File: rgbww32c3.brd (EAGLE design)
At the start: 36.8 x 20.3 mm, 21 parts, among them IC2 7805TV

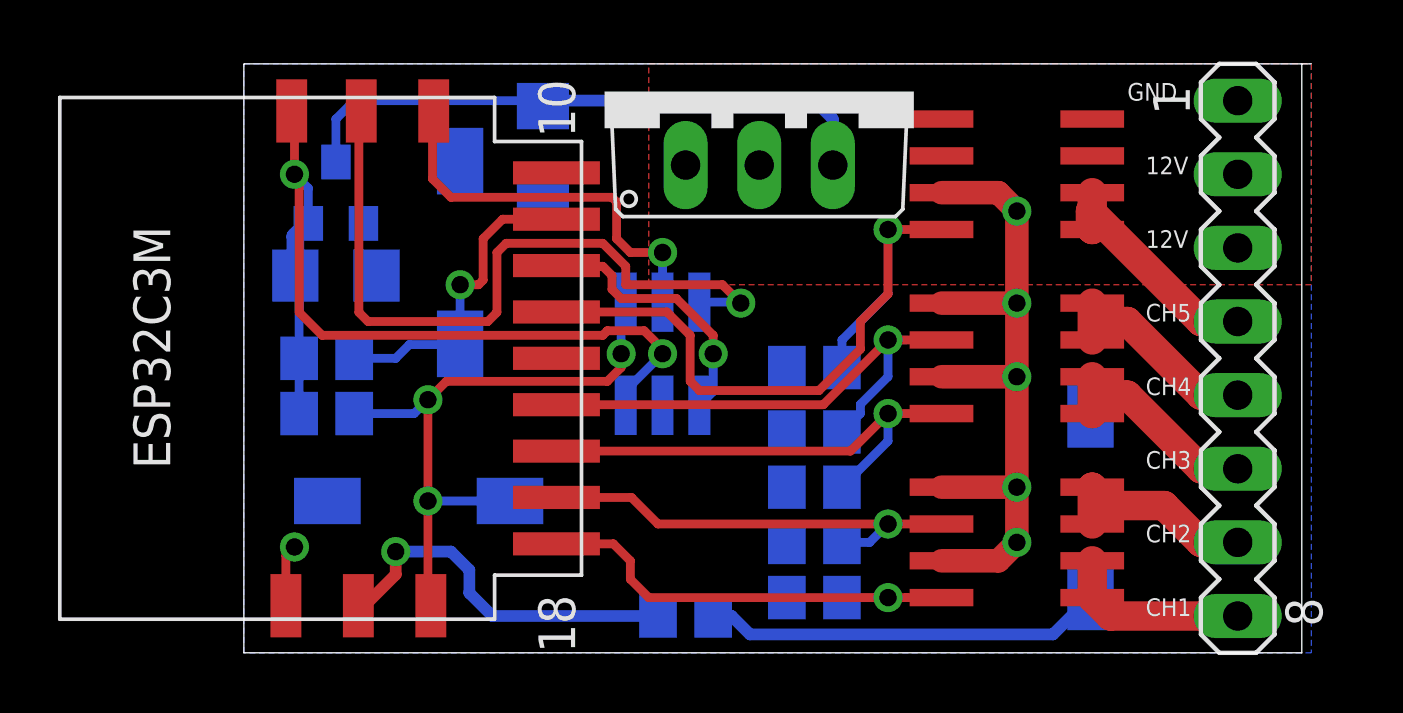
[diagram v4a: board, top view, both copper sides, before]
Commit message: few routing corrections to better avoid short circuits
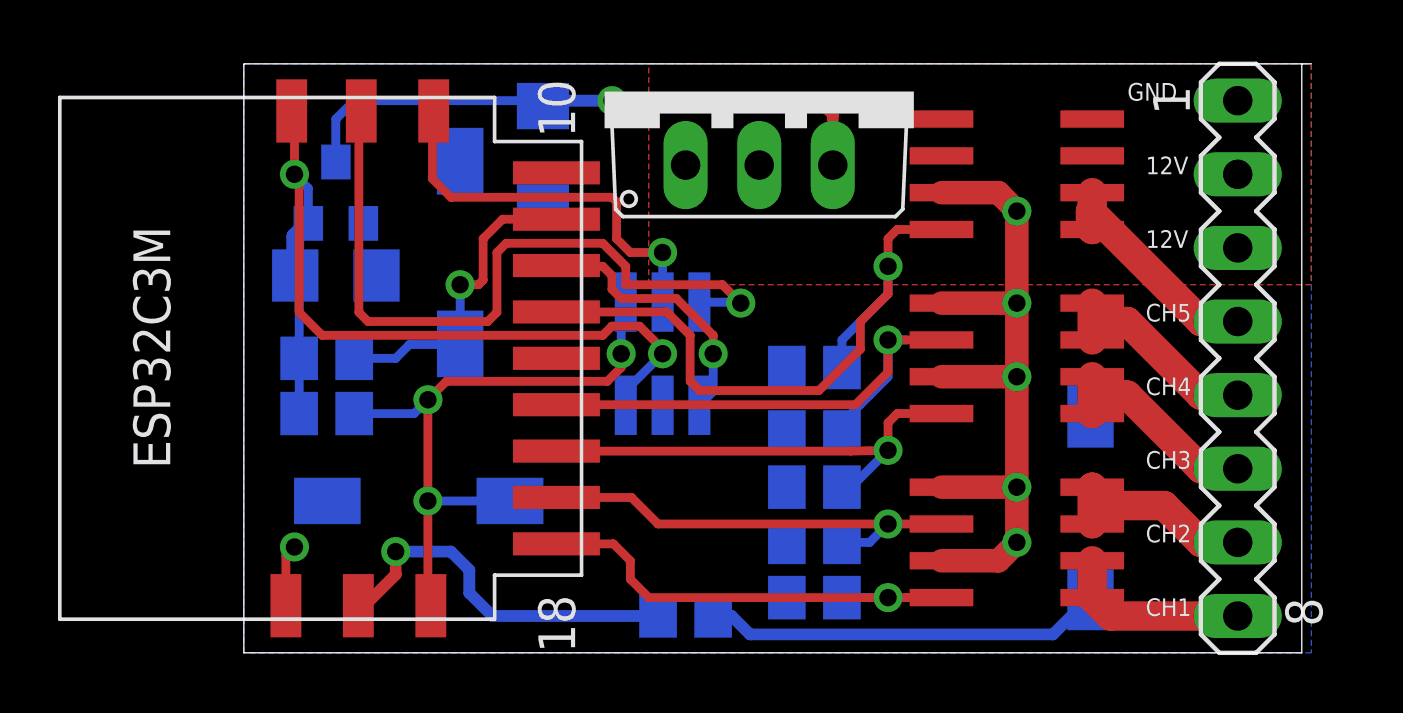
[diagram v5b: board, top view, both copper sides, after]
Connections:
- net CH1S: now also R4.1, U$1.4, U$5.GP10; no longer R3.1, U$1.2, U$5.GP7
- net CH2S: now also R3.1, U$1.2, U$5.GP7; no longer R4.1, U$1.4, U$5.GP10
- net CH3S: now also R2.1, U$2.4, U$5.GP6; no longer R5.1, U$2.2, U$5.GP5
- net CH4S: now also R5.1, U$2.2, U$5.GP5; no longer R2.1, U$2.4, U$5.GP6
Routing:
- net CH4S: track 17.0 -> 19.3 mm
- net CH3S: track 18.7 -> 16.5 mm
- net CH5S: track 24.9 -> 23.5 mm
- net 5V: track 21.0 -> 21.1 mm, vias 0 -> 1
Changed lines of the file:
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@@
 <contactref element="C2" pad="1"/>
 <wire x1="10.50625" y1="78.74" x2="10.31875" y2="78.5525" width="0.3048" layer="16"/>
-<wire x1="10.50625" y1="78.74" x2="19.685" y2="78.74" width="0.4064" layer="16"/>
-<wire x1="19.685" y1="78.74" x2="20.32" y2="78.105" width="0.4064" layer="16"/>
-<wire x1="20.32" y1="78.105" x2="20.32" y2="76.5175" width="0.4064" layer="16"/>
+<wire x1="10.50625" y1="78.74" x2="12.7" y2="78.74" width="0.4064" layer="16"/>
+<via x="12.7" y="78.74" extent="1-16" drill="0.6"/>
+<wire x1="12.7" y1="78.74" x2="19.84375" y2="78.74" width="0.4064" layer="1"/>
+<wire x1="19.84375" y1="78.74" x2="20.32" y2="78.26375" width="0.4064" layer="1"/>
+<wire x1="20.32" y1="78.26375" x2="20.32" y2="76.5175" width="0.4064" layer="1"/>
 </signal>
 <signal name="3V3">
@@
 <via x="14.44625" y="70.00875" extent="1-16" drill="0.6"/>
 <wire x1="14.44625" y1="70.00875" x2="14.44625" y2="70.1675" width="0.3048" layer="1"/>
-<wire x1="14.44625" y1="70.1675" x2="13.81125" y2="70.8025" width="0.3048" layer="1"/>
+<wire x1="14.44625" y1="70.1675" x2="13.6525" y2="70.96125" width="0.3048" layer="1"/>
 <wire x1="2.70125" y1="70.64375" x2="1.9075" y2="71.4375" width="0.3048" layer="1"/>
 <wire x1="1.9075" y1="71.4375" x2="1.9075" y2="76.03875" width="0.3048" layer="1"/>
 <wire x1="1.9075" y1="76.03875" x2="1.74625" y2="76.2" width="0.3048" layer="1"/>
-<wire x1="13.81125" y1="70.8025" x2="12.54125" y2="70.8025" width="0.3048" layer="1"/>
-<wire x1="12.54125" y1="70.8025" x2="12.3825" y2="70.64375" width="0.3048" layer="1"/>
+<wire x1="13.6525" y1="70.96125" x2="12.7" y2="70.96125" width="0.3048" layer="1"/>
+<wire x1="12.7" y1="70.96125" x2="12.3825" y2="70.64375" width="0.3048" layer="1"/>
 <wire x1="12.3825" y1="70.64375" x2="2.70125" y2="70.64375" width="0.3048" layer="1"/>
 <wire x1="1.775" y1="72.7075" x2="1.775" y2="74.055" width="0.6096" layer="16"/>
@@
 <via x="6.35" y="68.42125" extent="1-16" drill="0.6"/>
 </signal>
-<signal name="CH2S">
+<signal name="CH1S">
 <contactref element="R4" pad="1"/>
 <contactref element="U$1" pad="4"/>
@@
 <wire x1="22.225" y1="61.595" x2="20.635" y2="61.595" width="0.3048" layer="16"/>
 </signal>
-<signal name="CH1S">
+<signal name="CH2S">
 <contactref element="R3" pad="1"/>
 <contactref element="U$1" pad="2"/>
@@
 <wire x1="21.59" y1="63.5" x2="20.635" y2="63.5" width="0.3048" layer="16"/>
 </signal>
-<signal name="CH4S">
+<signal name="CH3S">
 <contactref element="R2" pad="1"/>
 <contactref element="U$2" pad="4"/>
 <contactref element="U$5" pad="GP6"/>
-<wire x1="24.07" y1="67.945" x2="22.225" y2="67.945" width="0.3048" layer="1"/>
-<via x="22.225" y="67.945" extent="1-16" drill="0.6"/>
+<via x="22.225" y="66.675" extent="1-16" drill="0.6"/>
 <wire x1="10.785" y1="66.65" x2="20.93" y2="66.65" width="0.3048" layer="1"/>
-<wire x1="20.93" y1="66.65" x2="22.225" y2="67.945" width="0.3048" layer="1"/>
-<wire x1="20.635" y1="65.405" x2="22.225" y2="66.995" width="0.3048" layer="16"/>
-<wire x1="22.225" y1="66.995" x2="22.225" y2="67.945" width="0.3048" layer="16"/>
+<wire x1="20.93" y1="66.65" x2="22.225" y2="66.675" width="0.3048" layer="1"/>
+<wire x1="24.07" y1="67.945" x2="22.5425" y2="67.945" width="0.3048" layer="1"/>
+<wire x1="22.5425" y1="67.945" x2="22.225" y2="67.6275" width="0.3048" layer="1"/>
+<wire x1="22.225" y1="67.6275" x2="22.225" y2="66.675" width="0.3048" layer="1"/>
+<wire x1="20.635" y1="65.405" x2="20.955" y2="65.405" width="0.3048" layer="16"/>
+<wire x1="20.955" y1="65.405" x2="22.225" y2="66.675" width="0.3048" layer="16"/>
 </signal>
-<signal name="CH3S">
+<signal name="CH4S">
 <contactref element="R5" pad="1"/>
 <contactref element="U$2" pad="2"/>
@@
 <wire x1="24.07" y1="70.485" x2="22.225" y2="70.485" width="0.3048" layer="1"/>
 <via x="22.225" y="70.485" extent="1-16" drill="0.6"/>
-<wire x1="10.785" y1="68.25" x2="19.99" y2="68.25" width="0.3048" layer="1"/>
-<wire x1="19.99" y1="68.25" x2="22.225" y2="70.485" width="0.3048" layer="1"/>
+<wire x1="10.785" y1="68.25" x2="21.10125" y2="68.25" width="0.3048" layer="1"/>
 <wire x1="22.225" y1="70.485" x2="22.86" y2="70.485" width="0.3048" layer="16"/>
-<wire x1="20.635" y1="67.31" x2="21.2725" y2="67.9475" width="0.3048" layer="16"/>
-<wire x1="21.2725" y1="67.9475" x2="21.2725" y2="68.2625" width="0.3048" layer="16"/>
-<wire x1="21.2725" y1="68.2625" x2="22.225" y2="69.215" width="0.3048" layer="16"/>
+<wire x1="21.2725" y1="68.2625" x2="21.59" y2="68.58" width="0.3048" layer="16"/>
+<wire x1="21.59" y1="68.58" x2="22.225" y2="69.215" width="0.3048" layer="16"/>
 <wire x1="22.225" y1="69.215" x2="22.225" y2="70.485" width="0.3048" layer="16"/>
+<wire x1="22.225" y1="70.485" x2="22.225" y2="69.37375" width="0.3048" layer="1"/>
+<wire x1="22.225" y1="69.37375" x2="21.10125" y2="68.25" width="0.3048" layer="1"/>
+<wire x1="20.635" y1="67.31" x2="20.635" y2="67.625" width="0.3048" layer="16"/>
+<wire x1="20.635" y1="67.625" x2="21.2725" y2="68.2625" width="0.3048" layer="16"/>
 </signal>
 <signal name="CH5S">
@@
 <contactref element="U$3" pad="4"/>
 <contactref element="U$5" pad="GP1"/>
-<wire x1="24.07" y1="74.295" x2="22.225" y2="74.295" width="0.3048" layer="1"/>
-<via x="22.225" y="74.295" extent="1-16" drill="0.6"/>
-<wire x1="22.225" y1="72.0725" x2="22.225" y2="74.295" width="0.3048" layer="16"/>
+<via x="22.225" y="73.025" extent="1-16" drill="0.6"/>
+<wire x1="22.225" y1="72.0725" x2="22.225" y2="73.025" width="0.3048" layer="16"/>
 <wire x1="20.635" y1="69.5325" x2="20.635" y2="70.4825" width="0.3048" layer="16"/>
 <wire x1="10.785" y1="71.45" x2="14.5925" y2="71.45" width="0.3048" layer="1"/>
@@
 <wire x1="21.2725" y1="70.1675" x2="21.2725" y2="71.12" width="0.3048" layer="1"/>
 <wire x1="21.2725" y1="71.12" x2="22.225" y2="72.0725" width="0.3048" layer="1"/>
-<wire x1="22.225" y1="72.0725" x2="22.225" y2="74.295" width="0.3048" layer="1"/>
+<wire x1="22.225" y1="72.0725" x2="22.225" y2="73.025" width="0.3048" layer="1"/>
+<wire x1="24.07" y1="74.295" x2="22.5425" y2="74.295" width="0.3048" layer="1"/>
+<wire x1="22.5425" y1="74.295" x2="22.225" y2="73.9775" width="0.3048" layer="1"/>
+<wire x1="22.225" y1="73.9775" x2="22.225" y2="73.025" width="0.3048" layer="1"/>
 </signal>
 <signal name="TX">
